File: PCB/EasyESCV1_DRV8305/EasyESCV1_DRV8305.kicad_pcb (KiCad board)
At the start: 2 copper layers, 11 parts, among them J2 TC2050-IDC, Q1 CSD16556Q5B, Q2 CSD16556Q5B, Q3 CSD16556Q5B, Q4 CSD16556Q5B, Q5 CSD16556Q5B, Q6 CSD16556Q5B, U1 DRV83053PHP, U2 TMS320F28027FPTT, U3 TPD4E05U06DQAR, U4 LMR16006XDDCR

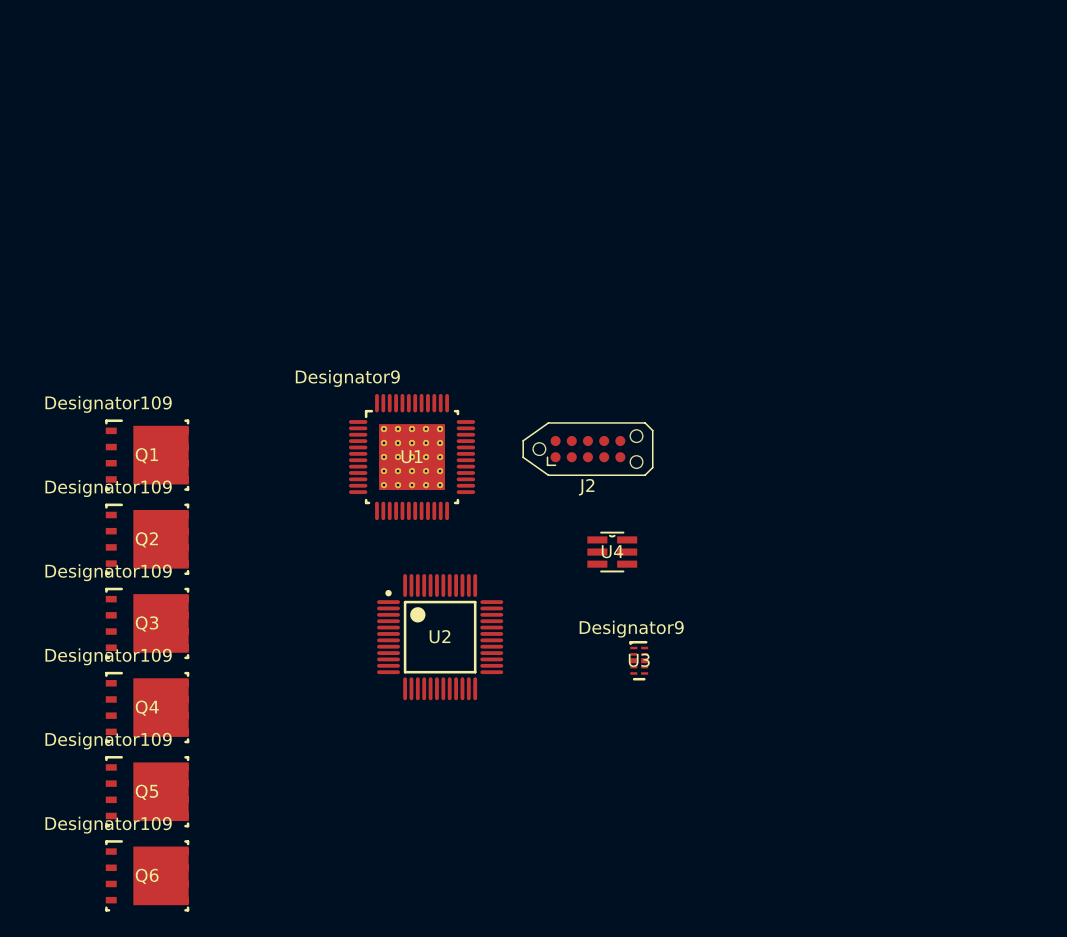
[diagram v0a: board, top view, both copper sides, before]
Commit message: Fixed issue with fet symbol and started layout
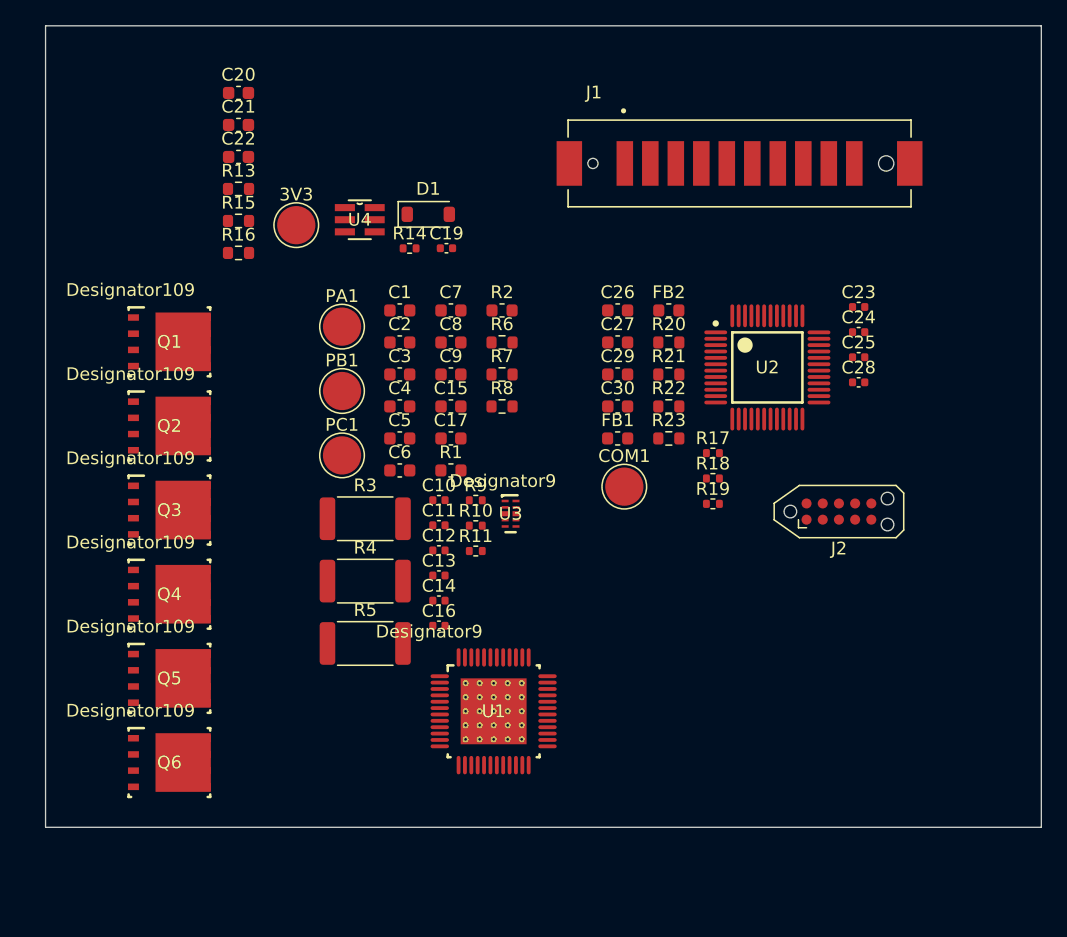
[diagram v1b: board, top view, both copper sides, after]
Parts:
- added 3V3: TestPoint, TestPoint:TestPoint_Pad_D3.0mm, F.Cu at (85.1, 52.5)
- added C1: 1u, Capacitor_SMD:C_0603_1608Metric, F.Cu at (93.2, 59.2)
- added C10: 0.1u, Capacitor_SMD:C_0402_1005Metric, F.Cu at (96.3, 74.0)
- added C11: 0.1u, Capacitor_SMD:C_0402_1005Metric, F.Cu at (96.3, 76.0)
- added C12: 0.1u, Capacitor_SMD:C_0402_1005Metric, F.Cu at (96.3, 78.0)
- added C13: 1n, Capacitor_SMD:C_0402_1005Metric, F.Cu at (96.3, 79.9)
- added C14: 1n, Capacitor_SMD:C_0402_1005Metric, F.Cu at (96.3, 81.9)
- added C15: 2.2u, Capacitor_SMD:C_0603_1608Metric, F.Cu at (97.2, 66.7)
- added C16: 1n, Capacitor_SMD:C_0402_1005Metric, F.Cu at (96.3, 83.9)
- added C17: 1u, Capacitor_SMD:C_0603_1608Metric, F.Cu at (97.2, 69.2)
- added C19: 0.1u, Capacitor_SMD:C_0402_1005Metric, F.Cu at (96.8, 54.3)
- added C2: 47n, Capacitor_SMD:C_0603_1608Metric, F.Cu at (93.2, 61.7)
- added C20: 0.33u, Capacitor_SMD:C_0603_1608Metric, F.Cu at (80.5, 42.1)
- added C21: 22u, Capacitor_SMD:C_0603_1608Metric, F.Cu at (80.5, 44.6)
- added C22: 1u, Capacitor_SMD:C_0603_1608Metric, F.Cu at (80.5, 47.1)
- added C23: 2.2n, Capacitor_SMD:C_0402_1005Metric, F.Cu at (129.2, 58.9)
- added C24: 2.2n, Capacitor_SMD:C_0402_1005Metric, F.Cu at (129.2, 60.9)
- added C25: 2.2n, Capacitor_SMD:C_0402_1005Metric, F.Cu at (129.2, 62.8)
- added C26: 2.2u, Capacitor_SMD:C_0603_1608Metric, F.Cu at (110.3, 59.2)
- added C27: 2.2u, Capacitor_SMD:C_0603_1608Metric, F.Cu at (110.3, 61.7)
- added C28: 0.1u, Capacitor_SMD:C_0402_1005Metric, F.Cu at (129.2, 64.8)
- added C29: 2.2u, Capacitor_SMD:C_0603_1608Metric, F.Cu at (110.3, 64.2)
- added C3: 1u, Capacitor_SMD:C_0603_1608Metric, F.Cu at (93.2, 64.2)
- added C30: 2.2u, Capacitor_SMD:C_0603_1608Metric, F.Cu at (110.3, 66.7)
- added C4: 1u, Capacitor_SMD:C_0603_1608Metric, F.Cu at (93.2, 66.7)
- added C5: 1u, Capacitor_SMD:C_0603_1608Metric, F.Cu at (93.2, 69.2)
- added C6: 1u, Capacitor_SMD:C_0603_1608Metric, F.Cu at (93.2, 71.7)
- added C7: 47n, Capacitor_SMD:C_0603_1608Metric, F.Cu at (97.2, 59.2)
- added C8: 1u, Capacitor_SMD:C_0603_1608Metric, F.Cu at (97.2, 61.7)
- added C9: 4.7u, Capacitor_SMD:C_0603_1608Metric, F.Cu at (97.2, 64.2)
- added COM1: TestPoint, TestPoint:TestPoint_Pad_D3.0mm, F.Cu at (110.8, 73.0)
- added D1: D_Schottky, Diode_SMD:D_SOD-123, F.Cu at (95.4, 51.6)
- added FB1: 600, Inductor_SMD:L_0603_1608Metric, F.Cu at (110.3, 69.2)
- added FB2: 600, Inductor_SMD:L_0603_1608Metric, F.Cu at (114.3, 59.2)
- added J1: 10159560-A00221RLF, Connectors:AMPHENOL_10159560-A00221RLF, F.Cu at (119.8, 47.6)
- added PA1: TestPoint, TestPoint:TestPoint_Pad_D3.0mm, F.Cu at (88.7, 60.4)
- added PB1: TestPoint, TestPoint:TestPoint_Pad_D3.0mm, F.Cu at (88.7, 65.5)
- added PC1: TestPoint, TestPoint:TestPoint_Pad_D3.0mm, F.Cu at (88.7, 70.5)
- added R1: 10K, Fuse:Fuse_0603_1608Metric, F.Cu at (97.2, 71.7)
- added R10: 4.99K, Resistor_SMD:R_0402_1005Metric, F.Cu at (99.2, 76.0)
- added R11: 4.99K, Resistor_SMD:R_0402_1005Metric, F.Cu at (99.2, 78.0)
- added R13: 24.9K, Resistor_SMD:R_0603_1608Metric, F.Cu at (80.5, 49.6)
- added R14: 4.99K, Resistor_SMD:R_0402_1005Metric, F.Cu at (94.0, 54.3)
- added R15: 68k, Resistor_SMD:R_0603_1608Metric, F.Cu at (80.5, 52.1)
- added R16: 20k, Resistor_SMD:R_0603_1608Metric, F.Cu at (80.5, 54.6)
- added R17: 56, Resistor_SMD:R_0402_1005Metric, F.Cu at (117.8, 70.3)
- added R18: 56, Resistor_SMD:R_0402_1005Metric, F.Cu at (117.8, 72.3)
- added R19: 56, Resistor_SMD:R_0402_1005Metric, F.Cu at (117.8, 74.3)
- added R2: 100, Fuse:Fuse_0603_1608Metric, F.Cu at (101.2, 59.2)
- added R20: 47K, Resistor_SMD:R_0603_1608Metric, F.Cu at (114.3, 61.7)
- added R21: 2.2K, Resistor_SMD:R_0603_1608Metric, F.Cu at (114.3, 64.2)
- added R22: 10K, Resistor_SMD:R_0603_1608Metric, F.Cu at (114.3, 66.7)
- added R23: 330, Resistor_SMD:R_0603_1608Metric, F.Cu at (114.3, 69.2)
- added R3: 0.007, Resistor_SMD:R_2512_6332Metric, F.Cu at (90.5, 75.5)
- added R4: 0.007, Resistor_SMD:R_2512_6332Metric, F.Cu at (90.5, 80.4)
- added R5: 0.007, Resistor_SMD:R_2512_6332Metric, F.Cu at (90.5, 85.3)
- added R6: 24.9K, Resistor_SMD:R_0603_1608Metric, F.Cu at (101.2, 61.7)
- added R7: 24.9K, Resistor_SMD:R_0603_1608Metric, F.Cu at (101.2, 64.2)
- added R8: 24.9K, Resistor_SMD:R_0603_1608Metric, F.Cu at (101.2, 66.7)
- added R9: 4.99K, Resistor_SMD:R_0402_1005Metric, F.Cu at (99.2, 74.0)
- moved U2 33.3 mm to (122.0, 63.6)
- moved U4 32.7 mm to (90.1, 52.0)
- moved U1 20.9 mm to (100.5, 90.6)
- moved J2 20.3 mm to (127.6, 74.9)
- moved U3 15.3 mm to (101.9, 75.1)
- moved Q2 9.06 mm to (75.1, 68.2)
- moved Q3 9.06 mm to (75.1, 74.8)
- moved Q4 9.06 mm to (75.1, 81.4)
- moved Q5 9.06 mm to (75.1, 88.0)
- moved Q6 9.06 mm to (75.1, 94.6)
- moved Q1 9.06 mm to (75.1, 61.6)
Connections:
- J2 pad 1: unconnected-(J2-Pin_1-Pad1) -> 3.3V
- J2 pad 2: unconnected-(J2-Pin_2-Pad2) -> TMS
- J2 pad 3: unconnected-(J2-Pin_3-Pad3) -> SP1
- J2 pad 4: unconnected-(J2-Pin_4-Pad4) -> TCK
- J2 pad 5: unconnected-(J2-Pin_5-Pad5) -> SP1
- J2 pad 6: unconnected-(J2-Pin_6-Pad6) -> TDO
- J2 pad 8: unconnected-(J2-Pin_8-Pad8) -> TDI
- J2 pad 9: unconnected-(J2-Pin_9-Pad9) -> nTRST
- Q1 pad 1: PVDD -> MOT_A
- Q1 pad 2: GH_A -> MOT_A
- Q1 pad 4: (no net) -> GH_A
- Q1 pad 5: (no net) -> PVDD
- Q1 pad 6: (no net) -> PVDD
- Q1 pad 7: (no net) -> PVDD
- Q1 pad 8: (no net) -> PVDD
- Q2 pad 1: MOT_A -> SL_A
- Q2 pad 2: GL_A -> SL_A
- Q2 pad 4: (no net) -> GL_A
- Q2 pad 5: (no net) -> MOT_A
- Q2 pad 6: (no net) -> MOT_A
- Q2 pad 7: (no net) -> MOT_A
- Q2 pad 8: (no net) -> MOT_A
- Q3 pad 1: PVDD -> MOT_B
- Q3 pad 2: GH_B -> MOT_B
- Q3 pad 4: (no net) -> GH_B
- Q3 pad 5: (no net) -> PVDD
- Q3 pad 6: (no net) -> PVDD
- Q3 pad 7: (no net) -> PVDD
- Q3 pad 8: (no net) -> PVDD
- Q4 pad 1: MOT_B -> SL_B
- Q4 pad 2: GL_B -> SL_B
- Q4 pad 4: (no net) -> GL_B
- Q4 pad 5: (no net) -> MOT_B
- Q4 pad 6: (no net) -> MOT_B
- Q4 pad 7: (no net) -> MOT_B
- Q4 pad 8: (no net) -> MOT_B
- Q5 pad 1: PVDD -> MOT_C
- Q5 pad 2: GH_C -> MOT_C
- Q5 pad 4: (no net) -> GH_C
- Q5 pad 5: (no net) -> PVDD
- Q5 pad 6: (no net) -> PVDD
- Q5 pad 7: (no net) -> PVDD
- Q5 pad 8: (no net) -> PVDD
- Q6 pad 1: MOT_C -> SL_C
- Q6 pad 2: GL_C -> SL_C
- Q6 pad 4: (no net) -> GL_C
- Q6 pad 5: (no net) -> MOT_C
- Q6 pad 6: (no net) -> MOT_C
- Q6 pad 7: (no net) -> MOT_C
- Q6 pad 8: (no net) -> MOT_C
- U2 pad 10: unconnected-(U2-ADCINA0_VREFHI-Pad10) -> VSEN_PVDD
- U2 pad 11: unconnected-(U2-VDDA-Pad11) -> VDDA
- U2 pad 12: unconnected-(U2-VSSA_VREFLO-Pad12) -> SP1
- U2 pad 13: unconnected-(U2-ADCINB1-Pad13) -> MCU_ISEN_A
- U2 pad 15: unconnected-(U2-ADCINB3-Pad15) -> MCU_ISEN_B
- U2 pad 18: unconnected-(U2-ADCINB7-Pad18) -> MCU_ISEN_C
- U2 pad 19: unconnected-(U2-GPIO34_COMP2OUT-Pad19) -> LED
- U2 pad 2: unconnected-(U2-TRST_N-Pad2) -> nTRST
- U2 pad 20: unconnected-(U2-GPIO35_TDI-Pad20) -> TDI
- U2 pad 21: unconnected-(U2-GPIO36_TMS-Pad21) -> TMS
- U2 pad 22: unconnected-(U2-GPIO37_TDO-Pad22) -> TDO
- U2 pad 23: unconnected-(U2-GPIO38_XCLKIN_TCK-Pad23) -> TCK
- U2 pad 24: unconnected-(U2-GPIO18_SPICLKA_SCITXDA_XCLKOUT-Pad24) -> SCLK
- U2 pad 25: unconnected-(U2-GPIO19_XCLKIN_SPISTEA_SCIRXDA_ECAP1_N-Pad25) -> COM
- U2 pad 26: unconnected-(U2-GPIO17_SPISOMIA_TZ3_N-Pad26) -> SDO
- U2 pad 27: unconnected-(U2-GPIO16_SPISIMOA_TZ2_N-Pad27) -> SDI
- U2 pad 28: unconnected-(U2-GPIO1_EPWM1B_COMP1OUT-Pad28) -> INL_A
- U2 pad 29: unconnected-(U2-GPIO0_EPWM1A-Pad29) -> INH_A
- U2 pad 3: unconnected-(U2-XRS_N-Pad3) -> nXRS
- U2 pad 32: unconnected-(U2-VDD-Pad32) -> Net-(C29-Pad1)
- U2 pad 33: unconnected-(U2-VSS-Pad33) -> SP1
- U2 pad 34: unconnected-(U2-VREGENZ_N-Pad34) -> SP1
- U2 pad 35: unconnected-(U2-VDDIO-Pad35) -> VDDIO
- U2 pad 36: unconnected-(U2-GPIO33_SCLA_EPWMSYNCO_ADCSOCBO_N-Pad36) -> nSCS
- U2 pad 37: unconnected-(U2-GPIO2_EPWM2A-Pad37) -> INH_B
- U2 pad 38: unconnected-(U2-GPIO3_EPWM2B_COMP2OUT-Pad38) -> INL_B
- U2 pad 39: unconnected-(U2-GPIO4_EPWM3A-Pad39) -> INH_C
- U2 pad 40: unconnected-(U2-GPIO5_EPWM3B_ECAP1-Pad40) -> INL_C
- U2 pad 41: unconnected-(U2-GPIO6_EPWM4A_EPWMSYNCI_EPWMSYNCO-Pad41) -> EN_GATE
- U2 pad 42: unconnected-(U2-GPIO7_EPWM4B_SCIRXDA-Pad42) -> WAKE
- U2 pad 43: unconnected-(U2-VDD-Pad43) -> Net-(C30-Pad1)
- U2 pad 44: unconnected-(U2-VSS-Pad44) -> SP1
- U2 pad 45: unconnected-(U2-X1-Pad45) -> SP1
- U2 pad 48: unconnected-(U2-GPIO28_SCIRXDA_SDAA_TZ2_N-Pad48) -> nFAULT
- U2 pad 6: unconnected-(U2-ADCINA7-Pad6) -> VSEN_A
- U2 pad 7: unconnected-(U2-ADCINA3-Pad7) -> VSEN_B
- U2 pad 8: unconnected-(U2-ADCINA1-Pad8) -> VSEN_C
- U4 pad 1: unconnected-(U4-CB-Pad1) -> Net-(U4-CB)
- U4 pad 2: unconnected-(U4-GND-Pad2) -> SP1
- U4 pad 3: unconnected-(U4-FB-Pad3) -> Net-(U4-FB)
- U4 pad 5: unconnected-(U4-VIN-Pad5) -> PVDD
- U4 pad 6: unconnected-(U4-SW-Pad6) -> Net-(D1-K)
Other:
- board outline added: 78.1 x 62.9 mm

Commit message: Started Layout
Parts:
- moved C24 131.6 mm to (113.3, 191.5)
- moved C23 130.6 mm to (112.5, 188.5)
- moved Q1 122.4 mm to (197.5, 62.2), turned to 180 degrees
- moved Q2 122.4 mm to (197.5, 68.8)
- moved Q3 122.4 mm to (197.5, 75.4), turned to 180 degrees
- moved Q4 122.4 mm to (197.5, 82.0)
- moved Q5 122.4 mm to (197.5, 88.6), turned to 180 degrees
- moved Q6 122.4 mm to (197.5, 95.2)
- moved C25 121.5 mm to (114.1, 183.4), turned to 180 degrees
- moved C27 119.9 mm to (108.5, 181.6), turned to -90 degrees
- moved FB2 119.3 mm to (108.5, 178.3), turned to -90 degrees
- moved C26 117.1 mm to (121.4, 175.8), turned to -90 degrees
- moved R23 117.0 mm to (115.6, 186.2)
- moved C29 115.4 mm to (121.4, 179.1), turned to -90 degrees
- moved R17 115.3 mm to (110.2, 185.4)
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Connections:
- net SP1 renamed GND
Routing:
- net GND: track 0.00 -> 15.3 mm, vias 0 -> 3
- net nTRST: track 0.00 -> 8.03 mm
- net VSEN_A: track 0.00 -> 4.88 mm, vias 0 -> 1
- net nXRS: track 0.00 -> 4.63 mm
- net VDDA: track 0.00 -> 4.30 mm
- net VDDIO: track 0.00 -> 4.18 mm
- net SCLK: track 0.00 -> 3.75 mm, vias 0 -> 1
- net VSEN_B: track 0.00 -> 3.67 mm, vias 0 -> 1
- net MCU_ISEN_C: track 0.00 -> 3.52 mm
- net Net-(C29-Pad1): track 0.00 -> 3.41 mm
- net TCK: track 0.00 -> 2.52 mm, vias 0 -> 1
- net VSEN_PVDD: track 0.00 -> 2.44 mm, vias 0 -> 1
- net VSEN_C: track 0.00 -> 2.44 mm, vias 0 -> 1
- net 3.3V: track 0.00 -> 1.69 mm
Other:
- board outline removed
- copper layers 2 -> 4
